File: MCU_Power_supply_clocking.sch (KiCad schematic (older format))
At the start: 59 parts, among them J2 OSTTC020162, U10 TLV75529PDBV, U11 STM32H743ZIT6, U12 LD1117S33CTR, U13 LD1117S33CTR, U9 ST1L05APU33R, Y1 NX5032GA-8MHz, Y2 NX3215SA-32.768K-STD-MUA-14

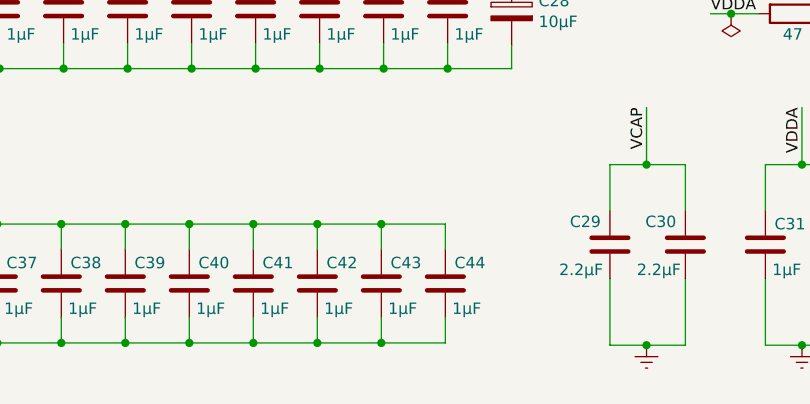
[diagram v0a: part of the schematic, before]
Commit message: PCB autorouting attempt
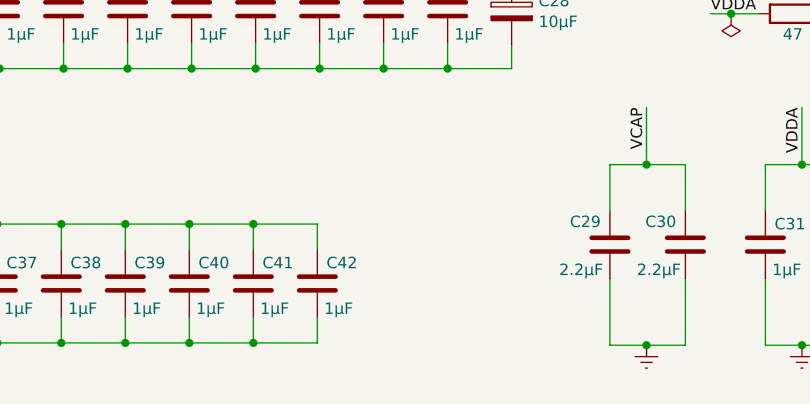
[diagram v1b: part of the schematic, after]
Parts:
- removed C43, C44: 1µF, Capacitor_SMD:C_0603_1608Metric_Pad1.08x0.95mm_HandSolder, symbol Device:C
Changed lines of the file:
@@
 	3220 7300 3220 7190
 Wire Wire Line
-	3500 7300 3500 7190
-Wire Wire Line
-	3780 7300 3780 7190
-Wire Wire Line
-	3780 7300 3500 7300
-Wire Wire Line
-	3500 7300 3220 7300
-Connection ~ 3500 7300
-Wire Wire Line
 	3220 7300 2940 7300
-Connection ~ 3220 7300
 Wire Wire Line
 	2940 7300 2660 7300
@@
 Connection ~ 1540 7300
 Wire Wire Line
-	3780 6780 3780 6890
-Wire Wire Line
-	3500 6780 3500 6890
-Wire Wire Line
 	3220 6780 3220 6890
 Wire Wire Line
@@
 	2940 6780 3220 6780
 Connection ~ 2940 6780
-Wire Wire Line
-	3220 6780 3500 6780
-Connection ~ 3220 6780
-Wire Wire Line
-	3500 6780 3780 6780
-Connection ~ 3500 6780
 Wire Wire Line
 	1260 7390 1260 7300
@@
 $EndComp
 $Comp
-L Device:C C?
-U 1 1 60A0FEC5
-P 3500 7040
-AR Path="/60A0FEC5" Ref="C?"  Part="1"
-AR Path="/60A03F8A/60A0FEC5" Ref="C43"  Part="1"
-F 0 "C43" H 3540 7130 50  0000 L CNN
-F 1 "1µF" H 3530 6930 50  0000 L CNN
-F 2 "Capacitor_SMD:C_0603_1608Metric_Pad1.08x0.95mm_HandSolder" H 3538 6890 50  0001 C CNN
-F 3 "http://www.farnell.com/datasheets/2710676.pdf" H 3500 7040 50  0001 C CNN
-F 4 "CL10B105KA8NNNC" H 3500 7040 50  0001 C CNN "Type"
-	1    3500 7040
-	1    0    0    -1
-$EndComp
-$Comp
 L power:GNDREF #PWR?
 U 1 1 60A0FEC7
@@
 	1    0    0    -1
 $EndComp
-$Comp
-L Device:C C?
-U 1 1 60A0FEC6
-P 3780 7040
-AR Path="/60A0FEC6" Ref="C?"  Part="1"
-AR Path="/60A03F8A/60A0FEC6" Ref="C44"  Part="1"
-F 0 "C44" H 3820 7130 50  0000 L CNN
-F 1 "1µF" H 3810 6930 50  0000 L CNN
-F 2 "Capacitor_SMD:C_0603_1608Metric_Pad1.08x0.95mm_HandSolder" H 3818 6890 50  0001 C CNN
-F 3 "http://www.farnell.com/datasheets/2710676.pdf" H 3780 7040 50  0001 C CNN
-F 4 "CL10B105KA8NNNC" H 3780 7040 50  0001 C CNN "Type"
-	1    3780 7040
-	1    0    0    -1
-$EndComp

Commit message: PCB layout
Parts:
- JP2: footprint Jumper:SolderJumper-2_P1.3mm_Open_TrianglePad1.0x1.5mm -> Connector_PinHeader_2.54mm:PinHeader_1x02_P2.54mm_Vertical
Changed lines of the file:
@@
 F 0 "JP2" H 10018 1468 60  0000 L CNN
 F 1 "JUMPER2" H 10018 1377 40  0000 L CNN
-F 2 "Jumper:SolderJumper-2_P1.3mm_Open_TrianglePad1.0x1.5mm" H 10040 1490 60  0001 C CNN
+F 2 "Connector_PinHeader_2.54mm:PinHeader_1x02_P2.54mm_Vertical" H 10040 1490 60  0001 C CNN
 F 3 "" H 10040 1490 60  0000 C CNN
 	1    10040 1490

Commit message: PCB minor changes
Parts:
- JP3: value Jumper_3_Bridged12 -> BOOT0
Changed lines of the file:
@@
 AR Path="/60A03F8A/60A2F808" Ref="JP3"  Part="1"
 F 0 "JP3" V 4650 3970 50  0000 L CNN
-F 1 "Jumper_3_Bridged12" V 4580 3990 50  0001 L CNN
+F 1 "BOOT0" V 4580 3990 50  0001 L CNN
 F 2 "Connector_PinHeader_2.54mm:PinHeader_1x03_P2.54mm_Horizontal" H 4590 3890 50  0001 C CNN
 F 3 "~" H 4590 3890 50  0001 C CNN

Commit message: PCB before Gerber creating
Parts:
- removed S1: KS-01Q-01_Obsolete, digikey-footprints:PushButton_Round_D12mm_THT_KS-01Q-01, symbol dk_Pushbutton-Switches:KS-01Q-01_Obsolete
- added SW7: RESET, Button_Switch_THT:SW_PUSH_6mm, symbol Switch:SW_Push
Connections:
- net GNDREF: now also SW7.2
- net NRST: now also SW7.1
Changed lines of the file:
@@
 	5340 6520 5510 6520
-Wire Wire Line
-	1430 3770 1300 3770
-Wire Wire Line
-	1300 3770 1300 3970
-Wire Wire Line
-	1430 3970 1300 3970
-Connection ~ 1300 3970
-Wire Wire Line
-	1300 3970 1300 4080
 Wire Wire Line
 	890  3770 1300 3770
@@
 Wire Wire Line
 	1300 4440 1960 4440
-Wire Wire Line
-	1960 4440 1960 3970
-Wire Wire Line
-	1960 3970 1830 3970
 Connection ~ 1300 4440
 Wire Wire Line
 	1300 4440 1300 4540
-Wire Wire Line
-	1830 3770 1960 3770
-Wire Wire Line
-	1960 3770 1960 3970
-Connection ~ 1960 3970
 Wire Wire Line
 	3380 1350 2910 1350
@@
 F 3 "" H 1300 4540 50  0001 C CNN
 	1    1300 4540
-	1    0    0    -1
-$EndComp
-$Comp
-L dk_Pushbutton-Switches:KS-01Q-01_Obsolete S?
-U 1 1 60A0FE98
-P 1630 3870
-AR Path="/60A0FE98" Ref="S?"  Part="1"
-AR Path="/60A03F8A/60A0FE98" Ref="S1"  Part="1"
-F 0 "S1" H 1630 4195 50  0000 C CNN
-F 1 "KS-01Q-01_Obsolete" H 1630 4104 50  0000 C CNN
-F 2 "digikey-footprints:PushButton_Round_D12mm_THT_KS-01Q-01" H 1830 4070 50  0001 L CNN
-F 3 "http://spec_sheets.e-switch.com/specs/29-KS01Q01.pdf" H 1830 4170 60  0001 L CNN
-F 4 "EG4791-ND" H 1830 4270 60  0001 L CNN "Digi-Key_PN"
-F 5 "KS-01Q-01" H 1830 4370 60  0001 L CNN "MPN"
-F 6 "Switches" H 1830 4470 60  0001 L CNN "Category"
-F 7 "Pushbutton Switches" H 1830 4570 60  0001 L CNN "Family"
-F 8 "http://spec_sheets.e-switch.com/specs/29-KS01Q01.pdf" H 1830 4670 60  0001 L CNN "DK_Datasheet_Link"
-F 9 "/product-detail/en/e-switch/KS-01Q-01/EG4791-ND/2116270" H 1830 4770 60  0001 L CNN "DK_Detail_Page"
-F 10 "SWITCH PUSH SPST-NO 0.01A 35V" H 1830 4870 60  0001 L CNN "Description"
-F 11 "E-Switch" H 1830 4970 60  0001 L CNN "Manufacturer"
-F 12 "Obsolete NonStock" H 1830 5070 60  0001 L CNN "Status"
-	1    1630 3870
 	1    0    0    -1
 $EndComp
@@
 Wire Wire Line
 	8360 5090 8690 5090
+$Comp
+L Switch:SW_Push SW7
+U 1 1 60CC4AC1
+P 1630 3770
+F 0 "SW7" H 1650 4090 50  0000 C CNN
+F 1 "RESET" H 1650 3990 50  0000 C CNN
+F 2 "Button_Switch_THT:SW_PUSH_6mm" H 1630 3970 50  0001 C CNN
+F 3 "~" H 1630 3970 50  0001 C CNN
+	1    1630 3770
+	1    0    0    -1
+$EndComp
+Wire Wire Line
+	1300 3770 1430 3770
+Wire Wire Line
+	1960 3770 1960 4440
+Wire Wire Line
+	1300 3770 1300 4080
+Wire Wire Line
+	1830 3770 1960 3770
 $EndSCHEMATC

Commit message: All mistakes corrected
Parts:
- Y1: footprint Crystal:Crystal_SMD_5032-2Pin_5.0x3.2mm_HandSoldering -> Crystal:Crystal_SMD_5032-2Pin_5.0x3.2mm
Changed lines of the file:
@@
 F 0 "Y1" V 3860 2140 50  0000 C CNN
 F 1 "NX5032GA-8MHz" V 3970 2220 50  0000 C CNN
-F 2 "Crystal:Crystal_SMD_5032-2Pin_5.0x3.2mm_HandSoldering" H 3760 2300 50  0001 C CNN
+F 2 "Crystal:Crystal_SMD_5032-2Pin_5.0x3.2mm" H 3760 2300 50  0001 C CNN
 F 3 "" H 3760 2300 50  0001 C CNN
 	1    3760 2300
